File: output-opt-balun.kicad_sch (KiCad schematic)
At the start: 10 parts, among them J2 SMA, T2 MABA-010247-2R1250

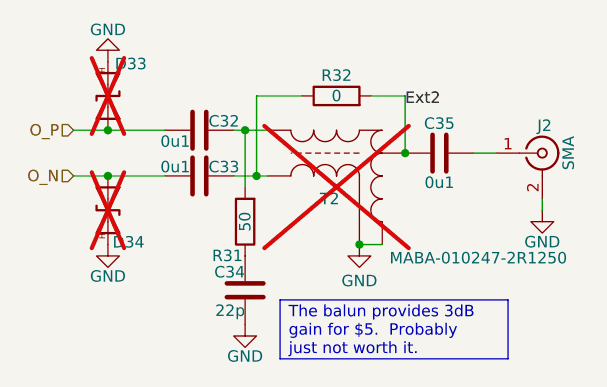
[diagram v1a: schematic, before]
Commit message: FPGA in, layout mostly updated.
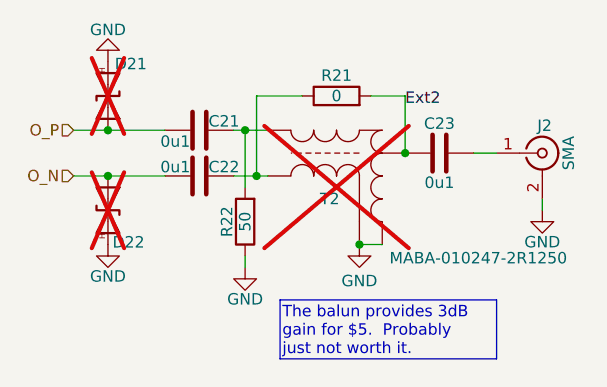
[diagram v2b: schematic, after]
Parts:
- removed C34: 22p, Capacitor_SMD:C_0402_1005Metric, symbol Device:C
- renumbered C32 to C21, C33 to C22, C35 to C23, D33 to D21, D34 to D22, R32 to R21, R31 to R22
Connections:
- net GND: now also R22.1
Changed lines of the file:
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@@
 		(exclude_from_sim no)
 		(at 153.7439 81.0839 0)
-		(size 25.3261 6.5461)
-		(margins 0.9525 0.9525 0.9525 0.9525)
+		(size 24.0561 6.5461)
+		(margins 0.254 0.254 0.254 0.254)
 		(stroke
 			(width 0)
@@
 		(pts
 			(xy 151.13 58.42) (xy 156.21 58.42)
+		)
+		(stroke
+			(width 0)
+			(type default)
+		)
+	)
+	(wire
+		(pts
+			(xy 149.86 76.2) (xy 149.86 77.47)
 		)
 		(stroke
@@
 		(in_pos_files yes)
 		(dnp no)
-		(property "Reference" "R32"
+		(property "Reference" "R21"
 			(at 160.02 56.896 90)
 			(show_name no)
@@
 			(project "gpsfreak"
 				(path "/3160ff17-81c2-4674-af97-e8d9acaf6b65/35d59e55-e2cb-40f2-90c1-a823bfbdd96c"
-					(reference "R32")
+					(reference "R21")
 					(unit 1)
 				)
@@
 		(in_pos_files yes)
 		(dnp no)
-		(property "Reference" "R31"
-			(at 149.606 75.438 0)
-			(show_name no)
-			(do_not_autoplace no)
-			(effects
-				(font
-					(size 1.27 1.27)
-				)
-				(justify left bottom)
+		(property "Reference" "R22"
+			(at 148.59 72.39 90)
+			(show_name no)
+			(do_not_autoplace no)
+			(effects
+				(font
+					(size 1.27 1.27)
+				)
+				(justify top)
 			)
 		)
@@
 			(project "gpsfreak"
 				(path "/3160ff17-81c2-4674-af97-e8d9acaf6b65/35d59e55-e2cb-40f2-90c1-a823bfbdd96c"
-					(reference "R31")
+					(reference "R22")
 					(unit 1)
 				)
@@
 		(in_pos_files yes)
 		(dnp yes)
-		(property "Reference" "D34"
+		(property "Reference" "D22"
 			(at 136.906 74.676 90)
 			(show_name no)
@@
 			(project "gpsfreak"
 				(path "/3160ff17-81c2-4674-af97-e8d9acaf6b65/35d59e55-e2cb-40f2-90c1-a823bfbdd96c"
-					(reference "D34")
+					(reference "D22")
 					(unit 1)
 				)
@@
 	(symbol
 		(lib_id "power:GND")
-		(at 149.86 83.82 0)
+		(at 149.86 77.47 0)
 		(unit 1)
 		(body_style 1)
@@
 		(dnp no)
 		(property "Reference" "#PWR095"
-			(at 149.86 90.17 0)
+			(at 149.86 83.82 0)
 			(hide yes)
 			(show_name no)
@@
 		)
 		(property "Value" "GND"
-			(at 149.86 86.614 0)
+			(at 149.86 80.264 0)
 			(show_name no)
 			(do_not_autoplace no)
@@
 		)
 		(property "Footprint" ""
-			(at 149.86 83.82 0)
+			(at 149.86 77.47 0)
 			(hide yes)
 			(show_name no)
@@
 		)
 		(property "Datasheet" ""
-			(at 149.86 83.82 0)
+			(at 149.86 77.47 0)
 			(hide yes)
 			(show_name no)
@@
 		)
 		(property "Description" "Power symbol creates a global label with name \"GND\" , ground"
-			(at 149.86 83.82 0)
+			(at 149.86 77.47 0)
 			(hide yes)
 			(show_name no)
@@
 		(in_pos_files yes)
 		(dnp no)
-		(property "Reference" "C32"
+		(property "Reference" "C21"
 			(at 145.796 61.976 90)
 			(show_name no)
@@
 			(project "gpsfreak"
 				(path "/3160ff17-81c2-4674-af97-e8d9acaf6b65/35d59e55-e2cb-40f2-90c1-a823bfbdd96c"
-					(reference "C32")
+					(reference "C21")
 					(unit 1)
 				)
@@
 		(in_pos_files yes)
 		(dnp no)
-		(property "Reference" "C33"
+		(property "Reference" "C22"
 			(at 145.796 67.056 90)
 			(show_name no)
@@
 			(project "gpsfreak"
 				(path "/3160ff17-81c2-4674-af97-e8d9acaf6b65/35d59e55-e2cb-40f2-90c1-a823bfbdd96c"
-					(reference "C33")
+					(reference "C22")
 					(unit 1)
 				)
@@
 		(in_pos_files yes)
 		(dnp no)
-		(property "Reference" "C35"
+		(property "Reference" "C23"
 			(at 171.45 62.23 90)
 			(show_name no)
@@
 			(project "gpsfreak"
 				(path "/3160ff17-81c2-4674-af97-e8d9acaf6b65/35d59e55-e2cb-40f2-90c1-a823bfbdd96c"
-					(reference "C35")
+					(reference "C23")
 					(unit 1)
 				)
@@
 		(in_pos_files yes)
 		(dnp yes)
-		(property "Reference" "D33"
+		(property "Reference" "D21"
 			(at 137.16 54.864 90)
 			(show_name no)
@@
 			(project "gpsfreak"
 				(path "/3160ff17-81c2-4674-af97-e8d9acaf6b65/35d59e55-e2cb-40f2-90c1-a823bfbdd96c"
-					(reference "D33")
+					(reference "D21")
 					(unit 1)
 				)
@@
 					(unit 1)
 				)
-			)
-		)
-	)
-	(symbol
-		(lib_id "Device:C")
-		(at 149.86 80.01 180)
-		(unit 1)
-		(body_style 1)
-		(exclude_from_sim no)
-		(in_bom yes)
-		(on_board yes)
-		(in_pos_files yes)
-		(dnp no)
-		(property "Reference" "C34"
-			(at 149.86 78.74 0)
-			(show_name no)
-			(do_not_autoplace no)
-			(effects
-				(font
-					(size 1.27 1.27)
-				)
-				(justify left top)
-			)
-		)
-		(property "Value" "22p"
-			(at 149.86 81.534 0)
-			(show_name no)
-			(do_not_autoplace no)
-			(effects
-				(font
-					(size 1.27 1.27)
-				)
-				(justify left bottom)
-			)
-		)
-		(property "Footprint" "Capacitor_SMD:C_0402_1005Metric"
-			(at 148.8948 76.2 0)
-			(hide yes)
-			(show_name no)
-			(do_not_autoplace no)
-			(effects
-				(font
-					(size 1.27 1.27)
-				)
-			)
-		)
-		(property "Datasheet" ""
-			(at 149.86 80.01 0)
-			(hide yes)
-			(show_name no)
-			(do_not_autoplace no)
-			(effects
-				(font
-					(size 1.27 1.27)
-				)
-			)
-		)
-		(property "Description" "Unpolarized capacitor"
-			(at 149.86 80.01 0)
-			(hide yes)
-			(show_name no)
-			(do_not_autoplace no)
-			(effects
-				(font
-					(size 1.27 1.27)
-				)
-			)
-		)
-		(property "LCSC" "C1555"
-			(at 149.86 80.01 90)
-			(hide yes)
-			(show_name no)
-			(do_not_autoplace no)
-			(effects
-				(font
-					(size 1.27 1.27)
-				)
-			)
-		)
-		(pin "1"
-		)
-		(pin "2"
-		)
-		(instances
-			(project "gpsfreak"
-				(path "/3160ff17-81c2-4674-af97-e8d9acaf6b65/35d59e55-e2cb-40f2-90c1-a823bfbdd96c"
-					(reference "C34")
-					(unit 1)
-				)

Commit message: Layout down
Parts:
- C21, C22, C23, R21: Stock (none) -> Basic
- D21, D22, T2: Stock (none) -> N/A
- J2: Stock (none) -> AliX
- R22: value 50 -> 49.9; Stock (none) -> Basic
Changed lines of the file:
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@@
+			)
+		)
+		(property "Stock" "Basic"
+			(at 160.02 58.42 90)
+			(hide yes)
+			(show_name no)
+			(do_not_autoplace no)
+			(effects
+				(font
+					(size 1.27 1.27)
+				)
 			)
 		)
@@
 			)
 		)
-		(property "Value" "50"
+		(property "Value" "49.9"
 			(at 149.86 72.39 90)
 			(show_name no)
@@
 		)
 		(property "LCSC" "C23185"
+			(at 149.86 72.39 90)
+			(hide yes)
+			(show_name no)
+			(do_not_autoplace no)
+			(effects
+				(font
+					(size 1.27 1.27)
+				)
+			)
+		)
+		(property "Stock" "Basic"
 			(at 149.86 72.39 90)
 			(hide yes)
@@
 		(property "Description" "Bidirectional transient-voltage-suppression diode"
 			(at 134.62 71.12 0)
+			(hide yes)
+			(show_name no)
+			(do_not_autoplace no)
+			(effects
+				(font
+					(size 1.27 1.27)
+				)
+			)
+		)
+		(property "Stock" "N/A"
+			(at 134.62 71.12 90)
 			(hide yes)
 			(show_name no)
@@
 			)
 		)
+		(property "Stock" "N/A"
+			(at 160.02 68.58 0)
+			(hide yes)
+			(show_name no)
+			(do_not_autoplace no)
+			(effects
+				(font
+					(size 1.27 1.27)
+				)
+			)
+		)
 		(pin "3"
 		)
@@
 			)
 		)
+		(property "Stock" "Basic"
+			(at 144.78 62.23 90)
+			(hide yes)
+			(show_name no)
+			(do_not_autoplace no)
+			(effects
+				(font
+					(size 1.27 1.27)
+				)
+			)
+		)
 		(pin "1"
 		)
@@
 			)
 		)
+		(property "Stock" "Basic"
+			(at 144.78 67.31 90)
+			(hide yes)
+			(show_name no)
+			(do_not_autoplace no)
+			(effects
+				(font
+					(size 1.27 1.27)
+				)
+			)
+		)
 		(pin "1"
 		)
@@
 			)
 		)
+		(property "Stock" "Basic"
+			(at 171.45 64.77 90)
+			(hide yes)
+			(show_name no)
+			(do_not_autoplace no)
+			(effects
+				(font
+					(size 1.27 1.27)
+				)
+			)
+		)
 		(pin "1"
 		)
@@
 		)
 		(property "Description" "coaxial connector (BNC, SMA, SMB, SMC, Cinch/RCA, LEMO, ...)"
+			(at 182.88 64.77 0)
+			(hide yes)
+			(show_name no)
+			(do_not_autoplace no)
+			(effects
+				(font
+					(size 1.27 1.27)
+				)
+			)
+		)
+		(property "Stock" "AliX"
 			(at 182.88 64.77 0)
 			(hide yes)
@@
 			(hide yes)
 			(show_name no)
+			(do_not_autoplace no)
+			(effects
+				(font
+					(size 1.27 1.27)
+				)
+			)
+		)
+		(property "Stock" "N/A"
+			(at 134.62 58.42 90)
+			(hide yes)
+			(show_name no)

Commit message: Adjustments.  Silk screen clearance.
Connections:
- net Ext2 renamed Ext
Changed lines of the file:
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@@
 		)
 	)
-	(label "Ext2"
+	(label "Ext"
 		(at 167.64 59.69 0)
 		(effects
